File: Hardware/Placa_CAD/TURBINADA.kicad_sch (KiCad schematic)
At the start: 33 parts, among them J1 TURBINA, J2 RESISTENCIAS, J3 BATERIA, U1 PIC16F18324-xSL

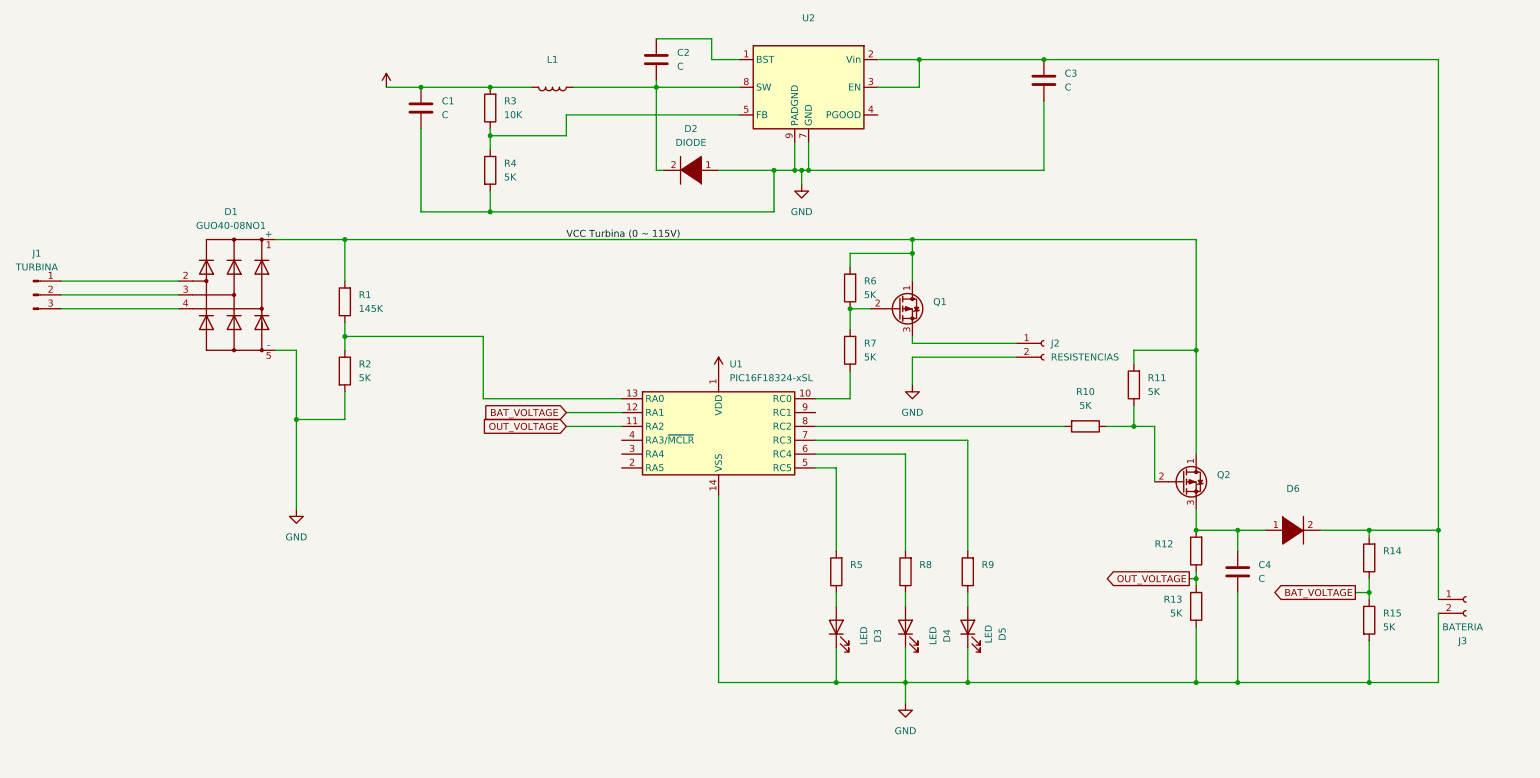
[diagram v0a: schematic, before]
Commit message: Selected transistor components in schematic
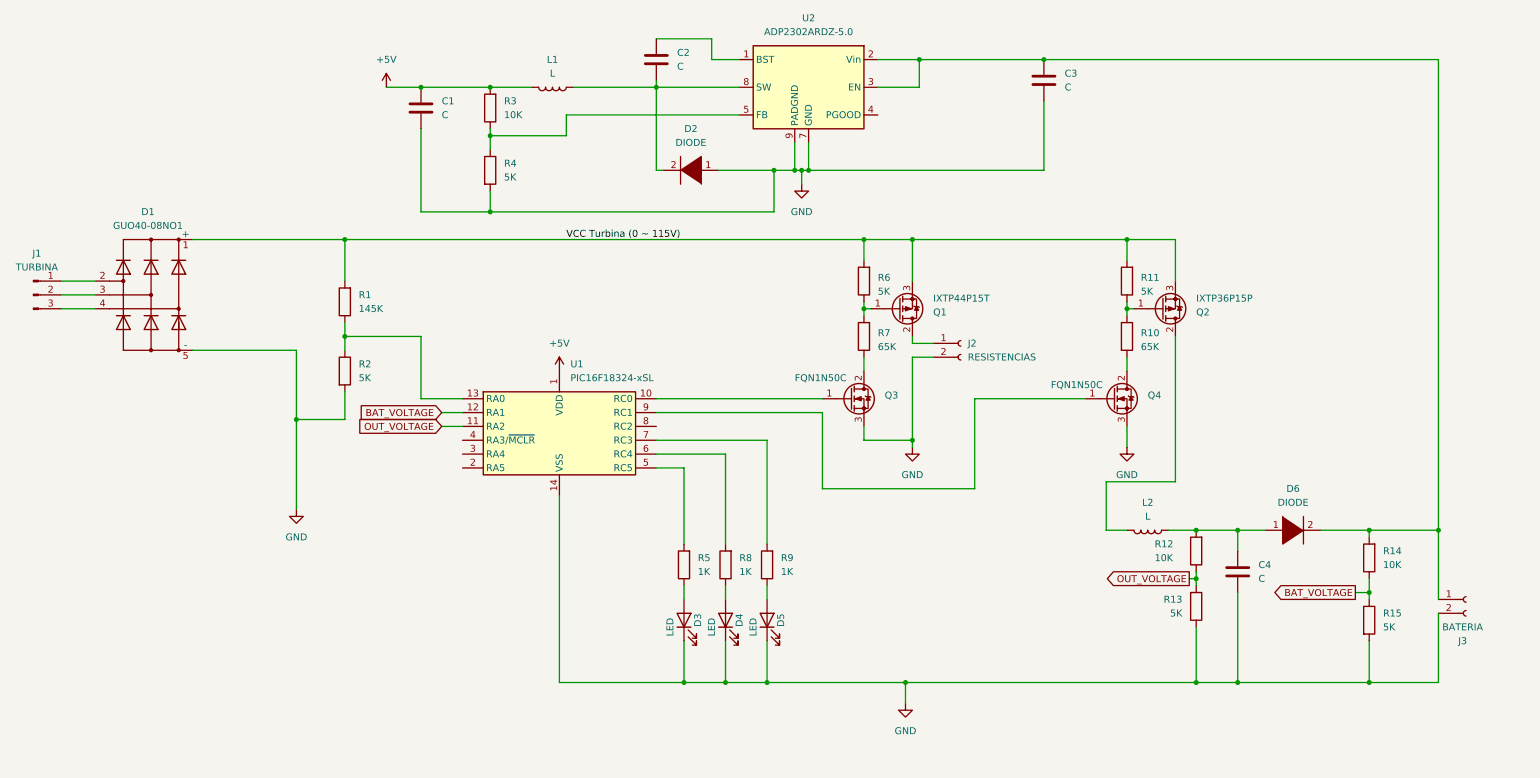
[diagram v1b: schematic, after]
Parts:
- removed Q1, Q2: (no value), symbol Device:Q_PMOS_DGS
- added L2: L, Inductor_THT:L_Axial_L5.3mm_D2.2mm_P2.54mm_Vertical_Vishay_IM-1, symbol Device:L
- added Q1: IXTP44P15T, Package_TO_SOT_THT:TO-220-3_Vertical, symbol Device:Q_PMOS_GDS
- added Q2: IXTP36P15P, Package_TO_SOT_THT:TO-220-3_Vertical, symbol Device:Q_PMOS_GDS
- added Q3, Q4: FQN1N50C, Package_TO_SOT_THT:TO-92, symbol Device:Q_NMOS_GDS
- C1, C2, C3, C4: footprint (none) -> Capacitor_THT:CP_Radial_D4.0mm_P1.50mm
- D2: footprint (none) -> Package_TO_SOT_THT:TO-92-2_Horizontal1
- D3, D4, D5: footprint (none) -> LED_THT:LED_D1.8mm_W3.3mm_H2.4mm
- D6: value (none) -> DIODE; footprint (none) -> Package_TO_SOT_THT:TO-92-2_Horizontal1
- J1: footprint (none) -> Connector_PinHeader_2.54mm:PinHeader_1x03_P2.54mm_Vertical
- J2, J3: footprint (none) -> Connector_PinHeader_2.54mm:PinHeader_1x02_P2.54mm_Vertical
- L1: value (none) -> L; footprint (none) -> Inductor_THT:L_Axial_L5.3mm_D2.2mm_P2.54mm_Vertical_Vishay_IM-1
- R1, R11, R13, R15, R2, R3, R4, R6: footprint (none) -> Resistor_THT:R_Axial_DIN0204_L3.6mm_D1.6mm_P7.62mm_Horizontal
- R10, R7: value 5K -> 65K; footprint (none) -> Resistor_THT:R_Axial_DIN0204_L3.6mm_D1.6mm_P7.62mm_Horizontal
- R12, R14: value (none) -> 10K; footprint (none) -> Resistor_THT:R_Axial_DIN0204_L3.6mm_D1.6mm_P7.62mm_Horizontal
- R5, R8, R9: value (none) -> 1K; footprint (none) -> Resistor_THT:R_Axial_DIN0204_L3.6mm_D1.6mm_P7.62mm_Horizontal
- U2: value (none) -> ADP2302ARDZ-5.0; footprint (none) -> Package_SO:SOIC-8-1EP_3.9x4.9mm_P1.27mm_EP2.29x3mm
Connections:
- net GND: now also Q3.3 (S), Q4.3 (S)
- net VCC Turbina (0 ~ 115V): now also Q1.3 (S), Q2.3 (S)
- net at R6.1, R7.2: now also Q1.1 (G)
- net at J2.1 (Pin_1): now also Q1.2 (D)
- net at R10.1, R11.1: now also Q2.1 (G)
- net at C4.1, D6.1 (K), R12.2: now also L2.1
- net at R10.2: now also Q4.2 (D); no longer U1.8 (RC2)
- net at U1.10 (RC0): now also Q3.1 (G); no longer R7.1
- net at U1.9 (RC1): now also Q4.1 (G)
- new net: L2.2, Q2.2 (D)
- new net: Q3.2 (D), R7.1
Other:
- moved on the sheet: D1, D3, D4, D5, J2, R10, R11, R5, R6, R7, R8, R9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

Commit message: Selected a few more components and footprints
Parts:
- added C5: 22uF, Capacitor_THT:CP_Radial_D4.0mm_P1.50mm, symbol Device:C
- added C6: 0.1uF, Capacitor_THT:C_Disc_D6.0mm_W4.4mm_P5.00mm, symbol Device:C
- added D7: DIODE, Diode_SMD:D_SMB_Handsoldering, symbol pspice:DIODE
- added R16: 78K, Resistor_THT:R_Axial_DIN0207_L6.3mm_D2.5mm_P7.62mm_Horizontal, symbol Device:R
- added R17: 10.2K, Resistor_THT:R_Axial_DIN0207_L6.3mm_D2.5mm_P7.62mm_Horizontal, symbol Device:R
- C1: value C -> 22uF
- C2: value C -> 0.1uF; footprint Capacitor_THT:CP_Radial_D4.0mm_P1.50mm -> Capacitor_THT:C_Disc_D6.0mm_W4.4mm_P5.00mm; Part (none) -> K104K15X7RF53H5
- C3: value C -> 10uF
- D1: Part (none) -> GUO40-08NO1
- D2: value DIODE -> SSB43L; footprint Package_TO_SOT_THT:TO-92-2_Horizontal1 -> Diode_SMD:D_SMB_Handsoldering; Part (none) -> SSB43L
- D3: value LED -> LED Green; footprint LED_THT:LED_D1.8mm_W3.3mm_H2.4mm -> LED_THT:LED_D4.0mm; Part (none) -> C4SMA-GGY-CU2W37A1
- D4: value LED -> LED Yellow; footprint LED_THT:LED_D1.8mm_W3.3mm_H2.4mm -> LED_THT:LED_D4.0mm; Part (none) -> SSL-LX3054OD
- D5: value LED -> LED Red; footprint LED_THT:LED_D1.8mm_W3.3mm_H2.4mm -> LED_THT:LED_D4.0mm; Part (none) -> C4SMA-RGY-CS4V1BB1
- L1: value L -> 6.8uH; footprint Inductor_THT:L_Axial_L5.3mm_D2.2mm_P2.54mm_Vertical_Vishay_IM-1 -> Inductor_SMD:L_Bourns_SRP1038C_10.0x10.0mm; Part (none) -> CLF10040T-6R8N-D
- R1: footprint Resistor_THT:R_Axial_DIN0204_L3.6mm_D1.6mm_P7.62mm_Horizontal -> Resistor_THT:R_Axial_DIN0207_L6.3mm_D2.5mm_P7.62mm_Horizontal; Part (none) -> CMF55145K00BER6
- R10, R7: footprint Resistor_THT:R_Axial_DIN0204_L3.6mm_D1.6mm_P7.62mm_Horizontal -> Resistor_THT:R_Axial_DIN0207_L6.3mm_D2.5mm_P7.62mm_Horizontal; Part (none) -> CMF5565K700BHEK
- R11, R13, R15, R2, R4, R6: footprint Resistor_THT:R_Axial_DIN0204_L3.6mm_D1.6mm_P7.62mm_Horizontal -> Resistor_THT:R_Axial_DIN0207_L6.3mm_D2.5mm_P7.62mm_Horizontal; Part (none) -> CMF555K0000BEEK
- R12, R14, R3: footprint Resistor_THT:R_Axial_DIN0204_L3.6mm_D1.6mm_P7.62mm_Horizontal -> Resistor_THT:R_Axial_DIN0207_L6.3mm_D2.5mm_P7.62mm_Horizontal; Part (none) -> CMF5510K000FKEK
- R5, R8, R9: footprint Resistor_THT:R_Axial_DIN0204_L3.6mm_D1.6mm_P7.62mm_Horizontal -> Resistor_THT:R_Axial_DIN0207_L6.3mm_D2.5mm_P7.62mm_Horizontal; Part (none) -> MF1/4LCT52R102J
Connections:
- net +5V: now also C5.2, C6.2
- net GND: now also C5.1, C6.1, D7.1 (K), R17.1; no longer U2.7 (GND), U2.9 (PADGND)
- net at C3.2, D6.2 (A), J3.1 (Pin_1)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: now also R16.2; no longer U2.3 (EN)
- net at L2.2, Q2.2 (D): now also D7.2 (A)
- new net: R16.1, R17.2, U2.3 (EN)
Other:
- moved on the sheet: C1, C3, D2, R12, R13

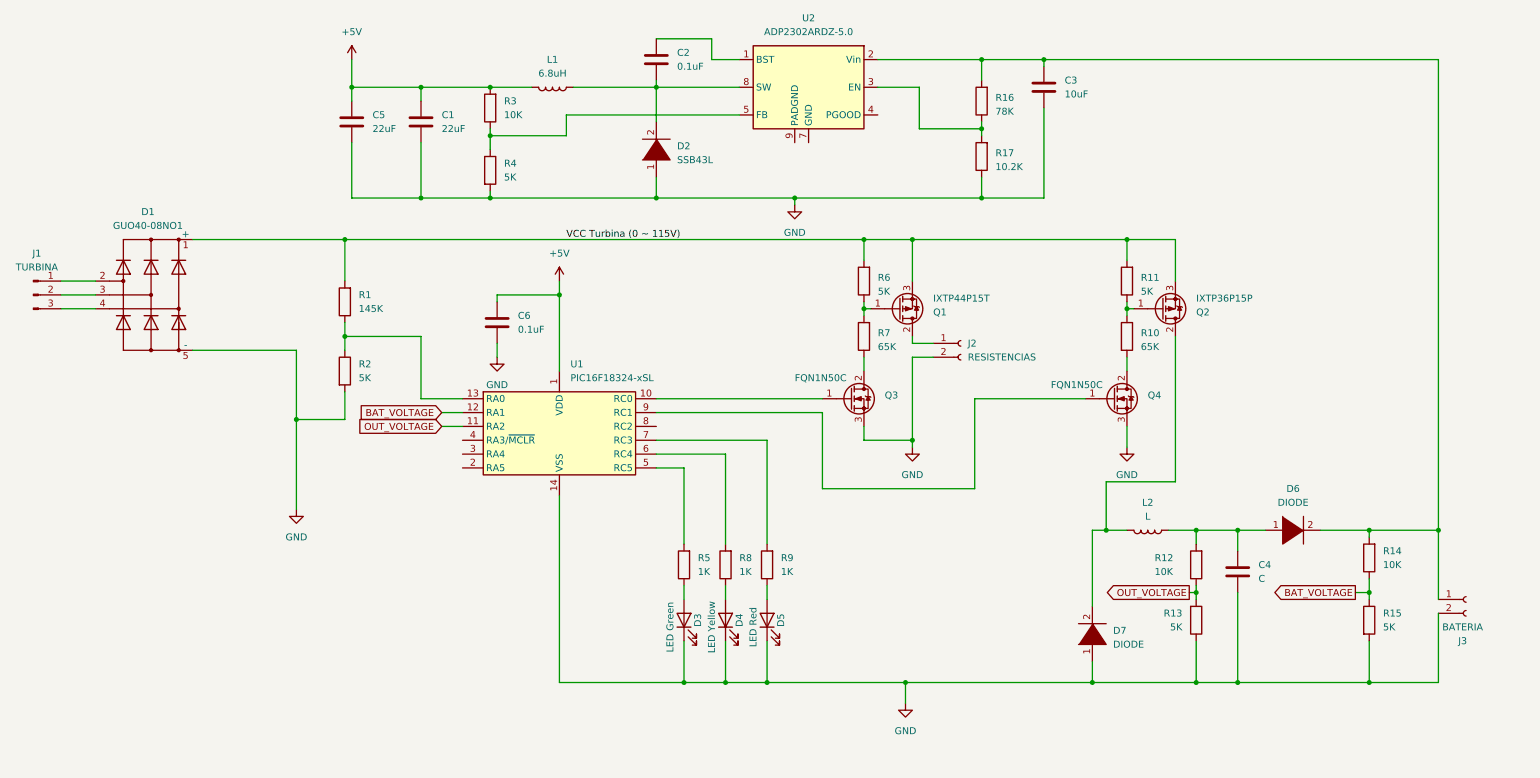
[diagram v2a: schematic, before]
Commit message: All components selected except for the output coil and capacitor
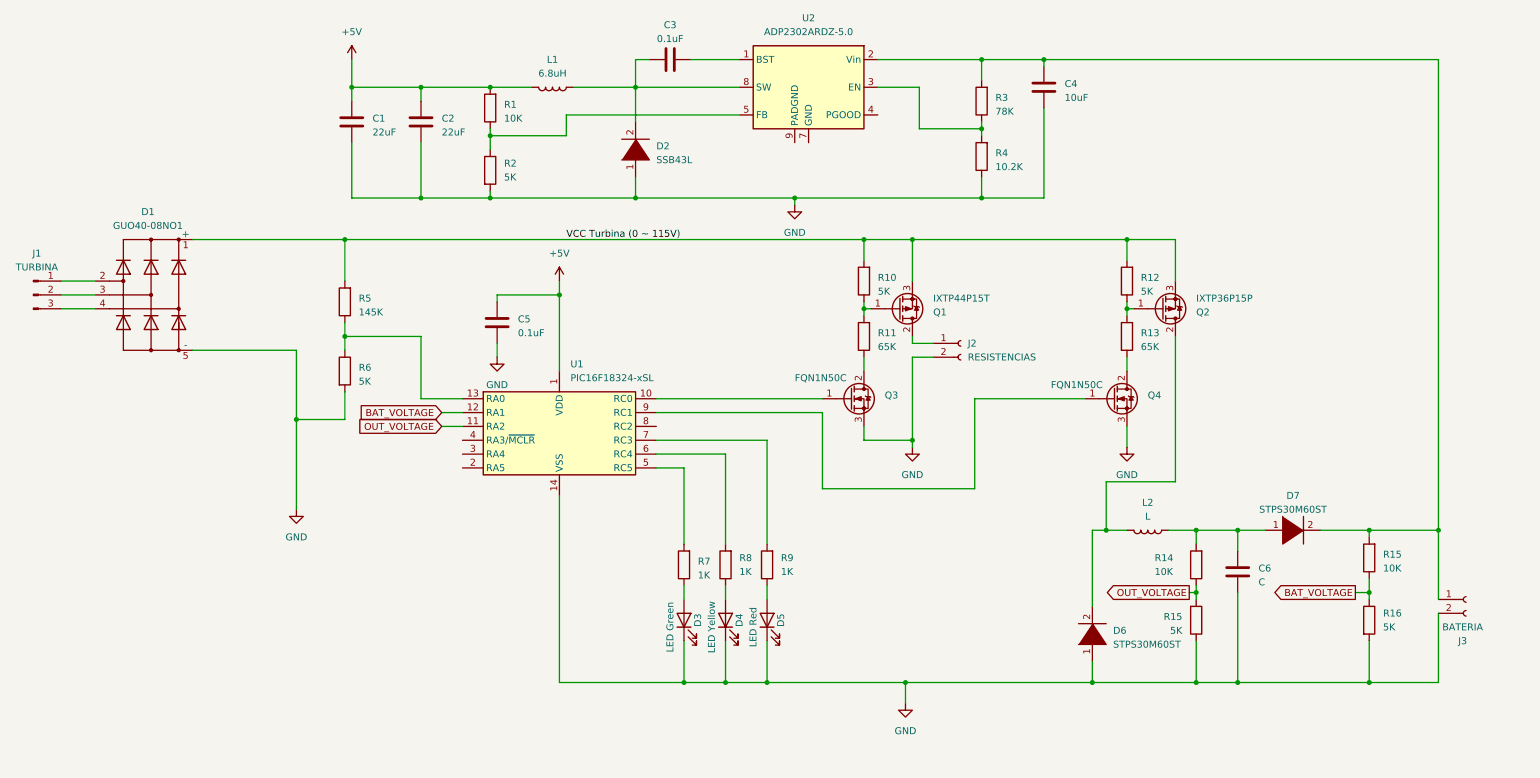
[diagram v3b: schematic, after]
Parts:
- C1: renamed from C5; footprint Capacitor_THT:CP_Radial_D4.0mm_P1.50mm -> Capacitor_THT:C_Disc_D7.5mm_W5.0mm_P5.00mm; Part (none) -> FG20X7R1C226MRT00
- C2: renamed from C1; footprint Capacitor_THT:CP_Radial_D4.0mm_P1.50mm -> Capacitor_THT:C_Disc_D7.5mm_W5.0mm_P5.00mm; Part (none) -> FG20X7R1C226MRT00
- C4: renamed from C3; footprint Capacitor_THT:CP_Radial_D4.0mm_P1.50mm -> Capacitor_THT:C_Disc_D6.0mm_W4.4mm_P5.00mm; Part (none) -> FG24X7R1A106KRT06
- D6: renamed from D7; value DIODE -> STPS30M60ST; footprint Diode_SMD:D_SMB_Handsoldering -> Package_TO_SOT_THT:TO-220-3_Vertical; Part (none) -> STPS30M60ST
- D7: renamed from D6; value DIODE -> STPS30M60ST; footprint Package_TO_SOT_THT:TO-92-2_Horizontal1 -> Package_TO_SOT_THT:TO-220-3_Vertical; Part (none) -> STPS30M60ST
- J1: footprint Connector_PinHeader_2.54mm:PinHeader_1x03_P2.54mm_Vertical -> Connector_Phoenix_GMSTB:PhoenixContact_GMSTBA_2,5_3-G_1x03_P7.50mm_Horizontal; Part (none) -> 1988118
- J2: footprint Connector_PinHeader_2.54mm:PinHeader_1x02_P2.54mm_Vertical -> Connector_Phoenix_MSTB:PhoenixContact_MSTBA_2,5_2-G_1x02_P5.00mm_Horizontal; Part (none) -> 1987724
- J3: footprint Connector_PinHeader_2.54mm:PinHeader_1x02_P2.54mm_Vertical -> TerminalBlock_RND:TerminalBlock_RND_205-00241_1x02_P10.16mm_Horizontal; Part (none) -> 1017526
- renumbered C2 to C3, C6 to C5, C4 to C6, R3 to R1, R6 to R10, R7 to R11, R11 to R12, R10 to R13, R12 to R14, R13 to R15, R14 to R15, R15 to R16, R4 to R2, R16 to R3, R17 to R4, R1 to R5, R2 to R6, R5 to R7
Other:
- moved on the sheet: C3, D2

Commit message: Selected all components. Started PCB drawing
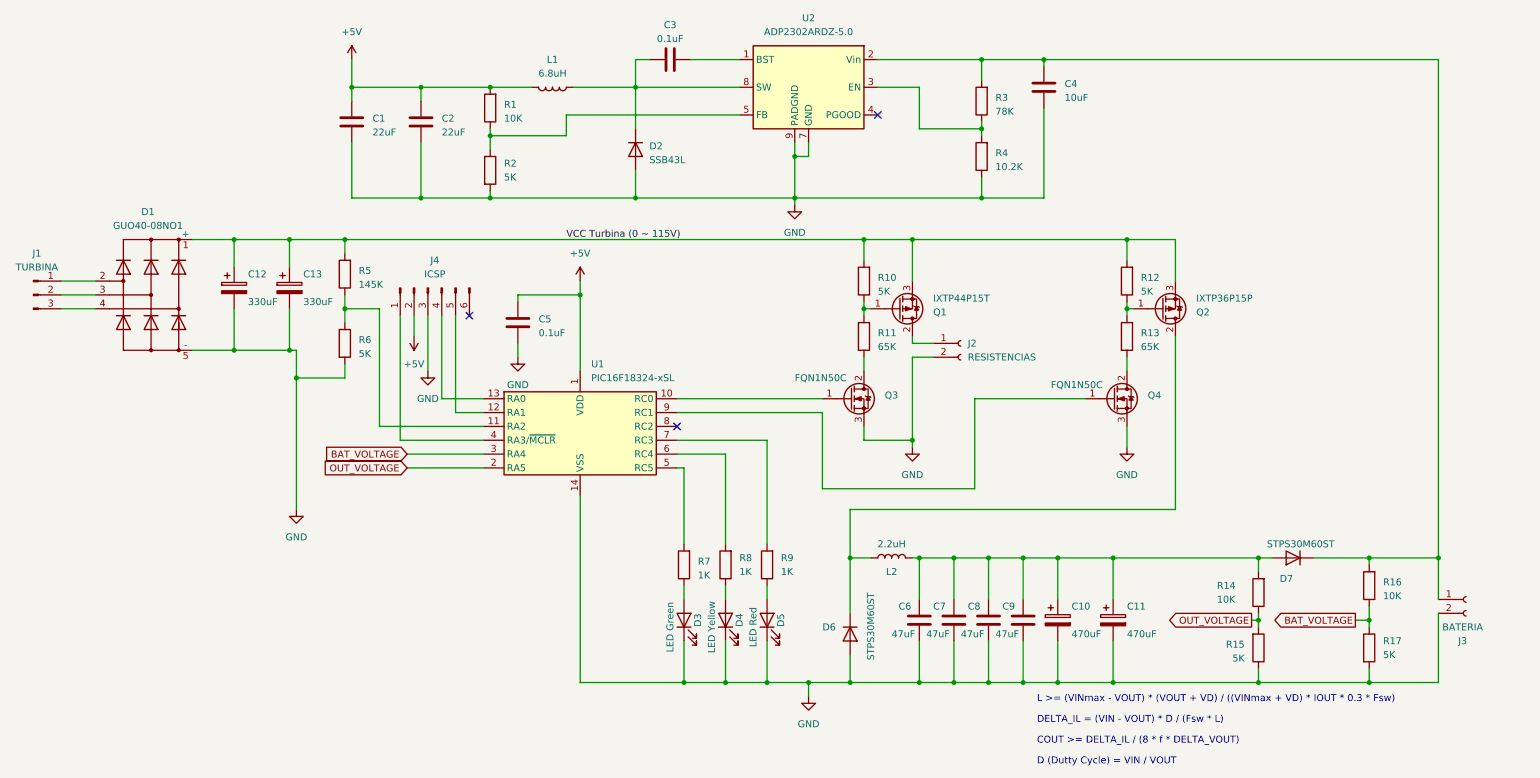
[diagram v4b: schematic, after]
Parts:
- removed D2: SSB43L, Diode_SMD:D_SMB_Handsoldering, symbol pspice:DIODE
- removed D6, D7: STPS30M60ST, Package_TO_SOT_THT:TO-220-3_Vertical, symbol pspice:DIODE
- added C10, C11: 470uF, Capacitor_THT:CP_Radial_D13.0mm_P5.00mm, symbol Device:C_Polarized
- added C12, C13: 330uF, Capacitor_THT:CP_Radial_D18.0mm_P7.50mm, symbol Device:C_Polarized
- added C7, C8, C9: 47uF, Capacitor_THT:C_Radial_D6.3mm_H5.0mm_P2.50mm, symbol Device:C
- added D2: SSB43L, Diode_SMD:D_SMB_Handsoldering, symbol Device:D
- added D6, D7: STPS30M60ST, Package_TO_SOT_THT:TO-220-3_Vertical, symbol Device:D
- added J4: ICSP, Connector_PinSocket_2.54mm:PinSocket_1x06_P2.54mm_Vertical, symbol Connector:Conn_01x06_Pin
- C6: value C -> 47uF; footprint Capacitor_THT:CP_Radial_D4.0mm_P1.50mm -> Capacitor_THT:C_Radial_D6.3mm_H5.0mm_P2.50mm; Part (none) -> FG16X5R1E476MRT06
- L2: value L -> 2.2uH; footprint Inductor_THT:L_Axial_L5.3mm_D2.2mm_P2.54mm_Vertical_Vishay_IM-1 -> footprints:IHXL1500VZEB1R5M51; Part (none) -> IHXL1500VZEB2R2M51
- U1: footprint Package_SO:SOIC-14_3.9x8.7mm_P1.27mm -> Package_DIP:DIP-14_W10.16mm
- renumbered R15 to R16, R16 to R17
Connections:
- net +5V: now also J4.2 (Pin_2)
- net BAT_VOLTAGE: now also U1.3 (RA4); no longer U1.12 (RA1)
- net GND: now also U2.7 (GND), U2.9 (PADGND), C10.2, C11.2, C12.2, C13.2, C7.2, C8.2, C9.2, D2.2 (A), D6.1 (A), D6.3 (A), J4.3 (Pin_3)
- net OUT_VOLTAGE: now also U1.2 (RA5); no longer U1.11 (RA2)
- net VCC Turbina (0 ~ 115V): now also C12.1, C13.1
- net at C3.1, L1.1, U2.8 (SW): now also D2.1 (K)
- net at C4.2, J3.1 (Pin_1), R16.2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: now also D7.2 (K)
- net at C6.1, R14.2: now also L2.3, C10.1, C11.1, C7.1, C8.1, C9.1, D7.1 (A), D7.3 (A); no longer L2.1
- net at Q2.2 (D): now also L2.1, D6.2 (K); no longer L2.2
- net at R5.1, R6.1: now also U1.11 (RA2); no longer U1.13 (RA0)
- net at U1.4 (RA3/~{MCLR}): now also J4.1 (Pin_1)
- new net: J4.4 (Pin_4), U1.13 (RA0)
- new net: J4.5 (Pin_5), U1.12 (RA1)
- no-connect marks 0 -> 3
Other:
- note added: "COUT >= DELTA_IL / (8 * f * DELTA_VOUT)"
- note added: "D (Dutty Cycle) = VIN / VOUT"
- note added: "DELTA_IL = (VIN - VOUT) * D / (Fsw * L)"
- note added: "L >= (VINmax - VOUT) * (VOUT + VD) / ((VINmax + VD) * IOUT * 0.3 * Fsw)"
- moved on the sheet: C5, C6, L2, R14, R15, R16, R17, R5, R6, U1

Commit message: Finished board layout
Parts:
- L2: footprint footprints:IHXL1500VZEB1R5M51 -> footprints:IHXL1500VZEB2R2M51
- R1: value 10K -> 52.3K; Part CMF5510K000FKEK -> MFR-25FBF52-52K3
- R2: value 5K -> 10K; Part CMF555K0000BEEK -> CMF5510K000FHEB
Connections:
- net at D6.2 (K), Q2.2 (D): now also L2.2; no longer L2.1
- net at C10.1, C11.1, C6.1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: now also L2.1; no longer L2.3
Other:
- moved on the sheet: L2
